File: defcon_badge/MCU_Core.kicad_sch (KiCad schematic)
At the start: 30 parts, among them J33 Dev/SWD header, U2 W25Q16JVUXIQ, U3 RP2040, Y1 ABM8-272-T3

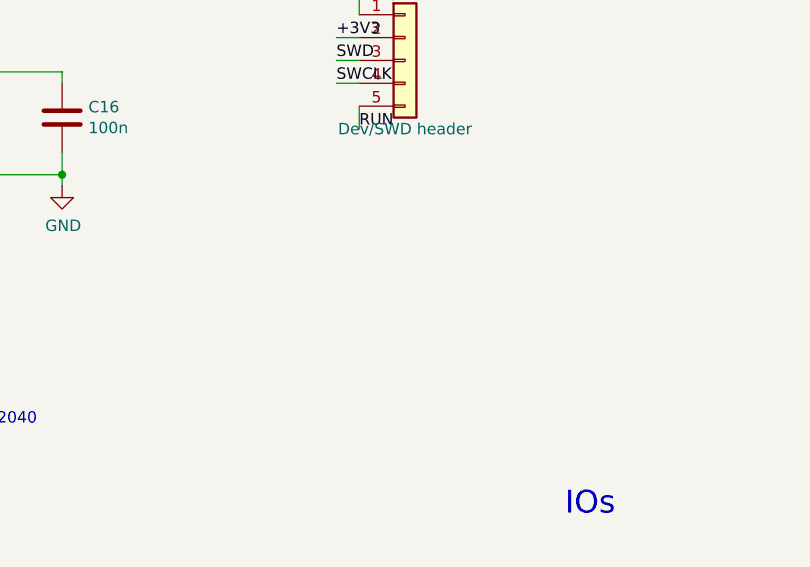
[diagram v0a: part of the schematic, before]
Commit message: Schematic: add RUN 10k pull-up (R6) + wrap-up
- RUN pull-up (R6, 10k RUN->+3V3) per badge_hw_design / RP2040 guide, via a new
  patch script tools/inject_mcu_passives.py (MCU_Core has no generator). Verified
  R6.1->+3V3, R6.2->RUN, ERC 0.
- ADC_AVDD filter: resolved as no-change — a direct ADC_AVDD<->3V3 tie is correct
  best-practice for the badge's coarse VBAT sensing (ferrite+cap only for precision).
- GPIO spares (GP22-25/27-29): waived (intentional unused pins).

Schematic is now electrically correct and ERC-error-clean: every board-killer and
subsystem-fatal bug (power tree, DAC pinout, LED pinout, charger EP) is fixed.
Remaining: microSD card-detect (cross-sheet feature, specced) + the PCB phase
(net re-sync, the SK9822-5050 / TP4056-ESOP8 / microSD-CD footprints, re-place).

Co-Authored-By: Claude Opus 4.8 (1M context) <noreply@anthropic.com>
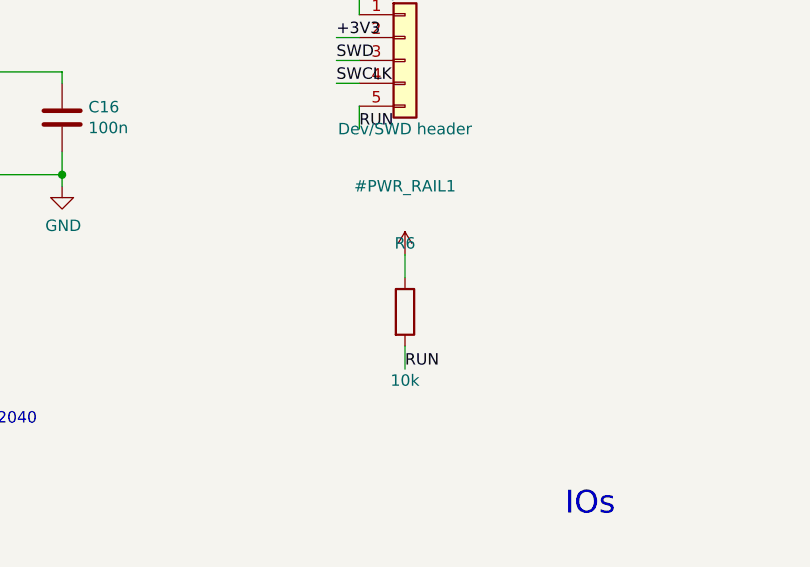
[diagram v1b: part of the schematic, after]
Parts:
- added R6: 10k, Resistor_SMD:R_0402_1005Metric, symbol Device:R
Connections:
- net +3V3: now also R6.1
- net RUN: now also R6.2
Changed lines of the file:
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@@
 		)
 	)
+	(symbol
+		(lib_id "Device:R")
+		(at 330.20 87.63 0)
+		(unit 1)
+		(body_style 1)
+		(exclude_from_sim no)
+		(in_bom yes)
+		(on_board yes)
+		(in_pos_files yes)
+		(dnp no)
+		(fields_autoplaced yes)
+		(property "Reference" "R6" (at 330.20 80.01 0) (effects (font (size 1.27 1.27))))
+		(property "Value" "10k" (at 330.20 95.25 0) (effects (font (size 1.27 1.27))))
+		(property "Footprint" "Resistor_SMD:R_0402_1005Metric" (at 330.20 87.63 0) (show_name no) (hide yes) (effects (font (size 1.27 1.27))))
+		(property "Datasheet" "" (at 330.20 87.63 0) (show_name no) (hide yes) (effects (font (size 1.27 1.27))))
+		(property "Description" "RUN pull-up to +3V3 (RP2040 reset noise immunity)" (at 330.20 87.63 0) (show_name no) (hide yes) (effects (font (size 1.27 1.27))))
+		(pin "1")
+		(pin "2")
+		(instances
+			(project "defcon_badge"
+				(path "/8c0b3d8b-46d3-4173-ab1e-a61765f77d61/614c6d9e-c93d-4105-a0eb-565eebb554cc"
+					(reference "R6")
+					(unit 1)
+				)
+			)
+		)
+	)
+	(symbol
+		(lib_id "power:+3V3")
+		(at 330.20 81.28 0)
+		(unit 1)
+		(body_style 1)
+		(exclude_from_sim no)
+		(in_bom yes)
+		(on_board yes)
+		(in_pos_files yes)
+		(dnp no)
+		(fields_autoplaced yes)
+		(property "Reference" "#PWR_RAIL1" (at 330.20 73.66 0) (effects (font (size 1.27 1.27))))
+		(property "Value" "+3V3" (at 330.20 88.90 0) (effects (font (size 1.27 1.27)) (hide yes)))
+		(property "Footprint" "" (at 330.20 81.28 0) (show_name no) (hide yes) (effects (font (size 1.27 1.27))))
+		(property "Datasheet" "" (at 330.20 81.28 0) (show_name no) (hide yes) (effects (font (size 1.27 1.27))))
+		(property "Description" "" (at 330.20 81.28 0) (show_name no) (hide yes) (effects (font (size 1.27 1.27))))
+		(pin "1")
+		(instances
+			(project "defcon_badge"
+				(path "/8c0b3d8b-46d3-4173-ab1e-a61765f77d61/614c6d9e-c93d-4105-a0eb-565eebb554cc"
+					(reference "#PWR_RAIL1")
+					(unit 1)
+				)
+			)
+		)
+	)
+	(wire (pts (xy 330.20 83.82) (xy 330.20 81.28)) (stroke (width 0) (type default)))
+	(wire (pts (xy 330.20 91.44) (xy 330.20 93.98)) (stroke (width 0) (type default)))
+	(label "RUN" (at 330.20 93.98 0) (effects (font (size 1.27 1.27)) (justify left bottom)))
 )

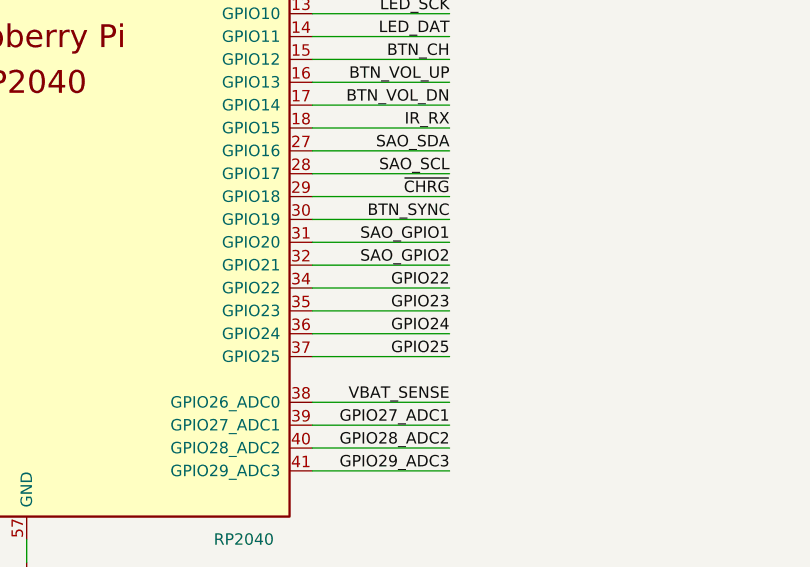
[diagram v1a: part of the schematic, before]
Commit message: Schematic: wire microSD card-detect (SD_CD) + add generator global-label support
Card-detect was unwired ("not wired this rev"). Wired it as a cross-sheet net:
- gen_io_sheet: J31.9 (DET) -> SD_CD with a 10k pull-up (R42) to +3V3. The DET
  switch shorts pin 9 to the grounded shield when a card is inserted, so SD_CD
  reads LOW = card present.
- MCU_Core: repurposed the GP22 spare (U3.34) for SD_CD.
- kicad_sheet_gen: add global-label support (global_label_at_pin / _render_global).
  Used a global label so SD_CD connects across the hierarchy without editing the
  top sheet's sheet-pins/wiring.

Verified: SD_CD = {J31.9, R42.1, U3.34}, R42.2->+3V3, ERC 0 errors.

SCHEMATIC COMPLETE: ERC 0 errors, all board-killers + subsystem-fatal bugs fixed,
4/5 sch_health gates pass (5th = waived GPIO spares). Remaining is the PCB phase.

Co-Authored-By: Claude Opus 4.8 (1M context) <noreply@anthropic.com>
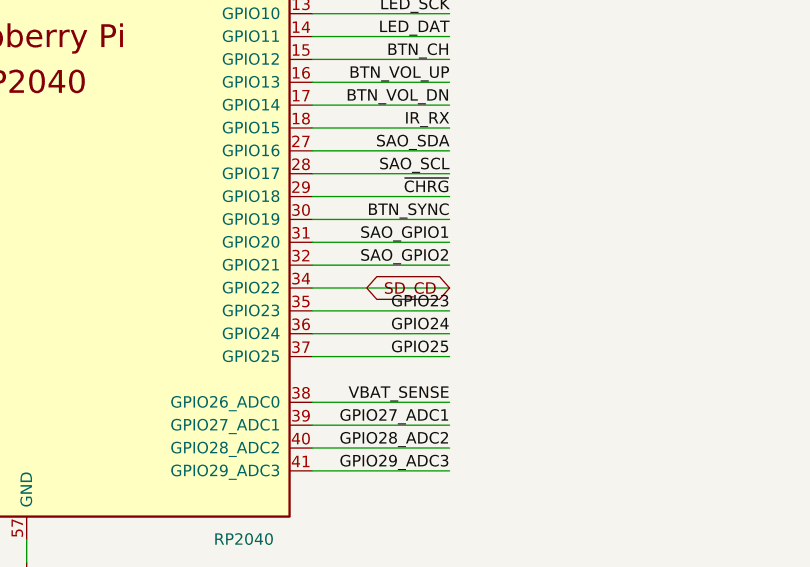
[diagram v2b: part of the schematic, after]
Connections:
- net GPIO22 renamed SD_CD
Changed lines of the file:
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@@
 		)
 	)
-	(label "GPIO22"
+	(global_label "SD_CD"
+		(shape bidirectional)
 		(at 245.11 167.64 180)
 		(effects
@@
 				(size 1.27 1.27)
 			)
-			(justify right bottom)
+			(justify right)
 		)
 	)

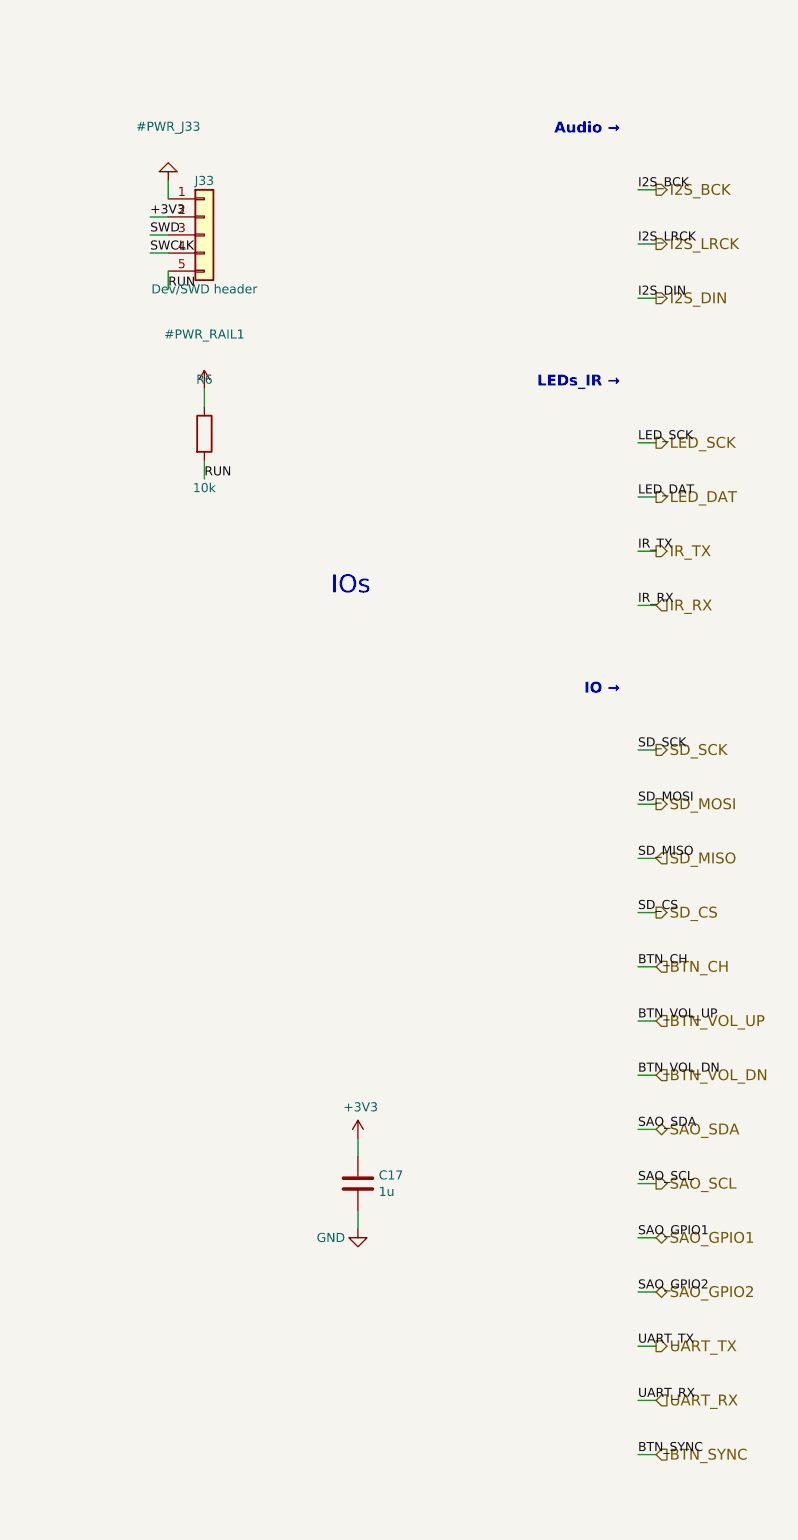
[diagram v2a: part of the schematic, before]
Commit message: Schematic: remove unused J32/J33 debug headers (user request)
The UART debug header (J32, IO sheet) and SWD debug header (J33, MCU_Core)
are unused — the RP2040 is programmed via BOOTSEL/USB (TP1/TP2 pogo pads),
so neither was ever placed on the PCB. Removed both from the schematic so
schematic↔PCB parity stays clean.

Done via a new surgical tool (tools/remove_dev_headers.py) that deletes the
symbols, their power/labels/wires, and the cross-sheet UART plumbing (IO
hier-labels + top-sheet sheet pins + MCU_Core hier-labels/stubs) by
top-level S-expression element, preserving every other symbol UUID (so the
PCB footprint linkage is untouched — no re-sync needed).

The RP2040 debug pins (SWCLK/SWDIO) and UART pins (GP0/GP1) keep their
labels as documented single-pin nets so future test points can attach.

Verified: kicad-cli ERC 0 errors, schematic parity 0 issues. Net warning
delta vs baseline: +4 isolated_pin_label (the intended documented debug
pins), -2 endpoint_off_grid; everything else unchanged.

Co-Authored-By: Claude Opus 4.8 (1M context) <noreply@anthropic.com>
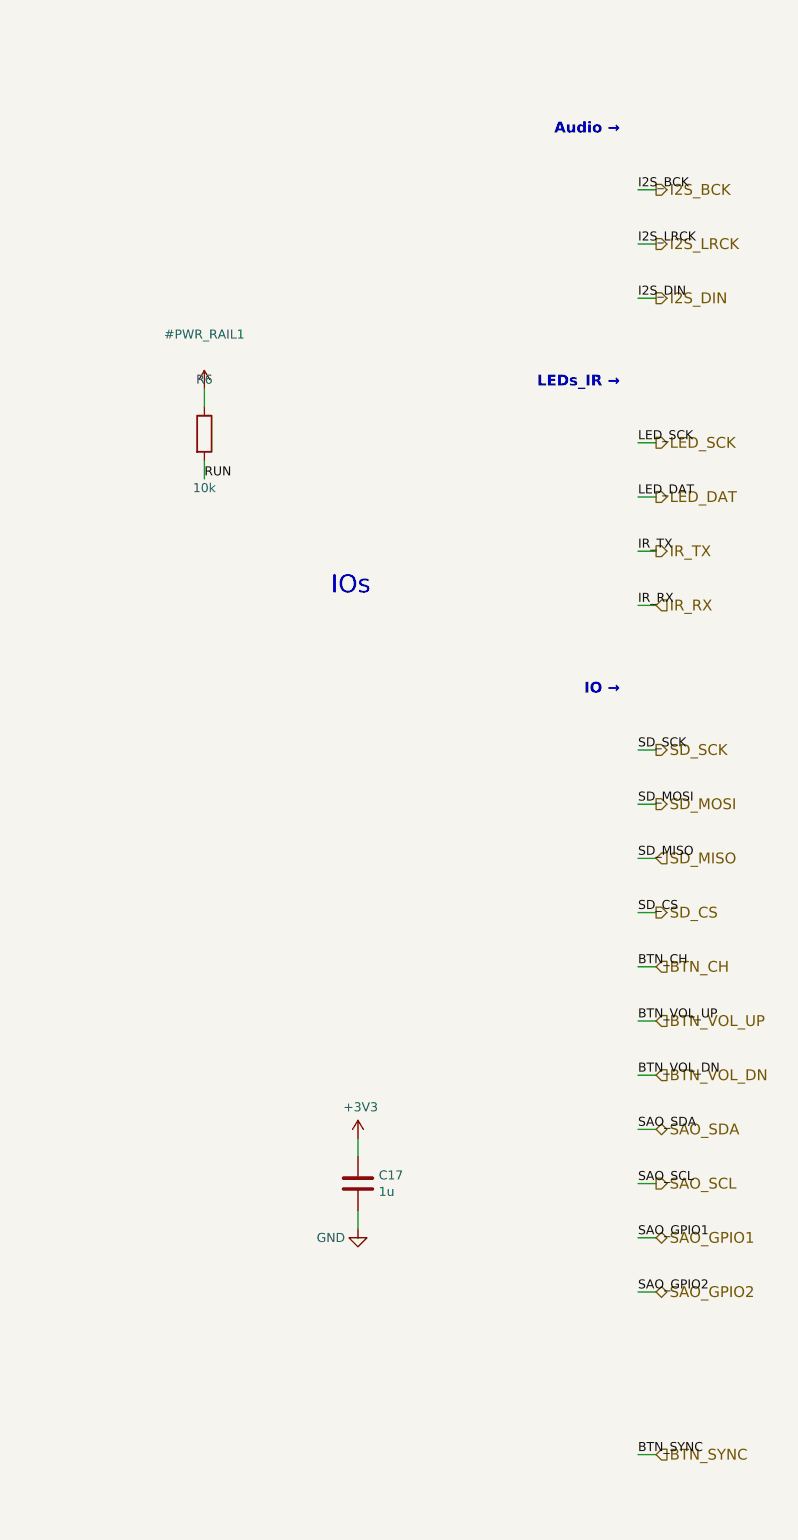
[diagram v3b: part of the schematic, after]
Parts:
- removed J33: Dev/SWD header, Connector_PinHeader_2.54mm:PinHeader_1x05_P2.54mm_Vertical, symbol Connector_Generic:Conn_01x05

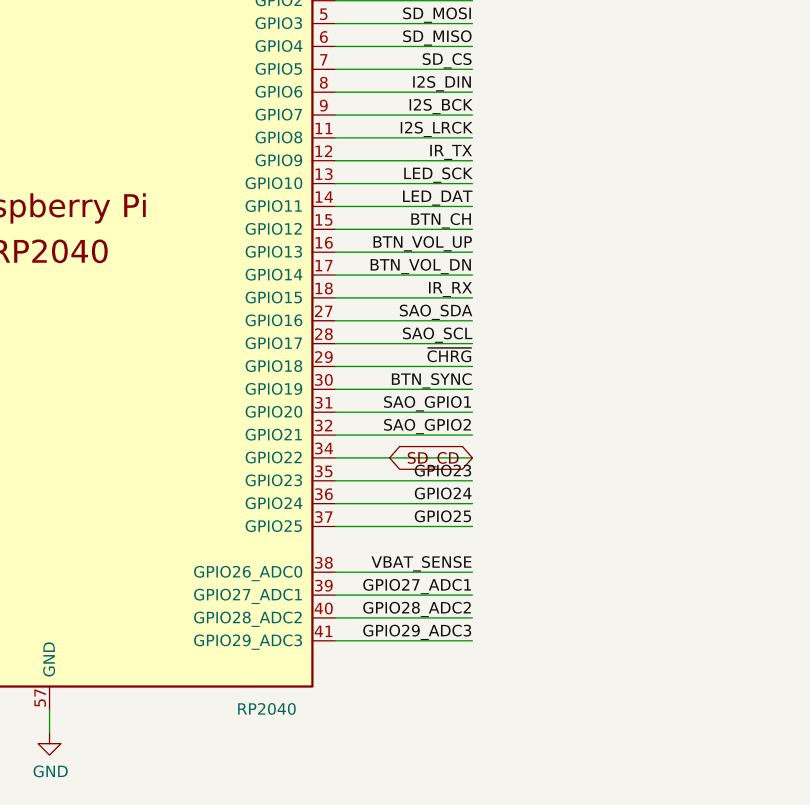
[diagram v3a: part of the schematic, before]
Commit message: R2(1): GPIO remap applied — 6 nets to destination-facing pins (schematic + PCB)
User-authorized firmware-flexible pin remap to dissolve the worst QFN escape
crossings at the source. Built solver (Hungarian + opposite-side penalty + RP2040
pinmux constraints), connectivity resolver (union-find, cross-checked 40/43 pins
vs PCB), and a label-permutation applier (only semantically-correct remap on a
function-named symbol). Moves: LED_SCK GP10->24, LED_DAT GP11->25, IR_RX GP15->27,
SAO_SDA GP16->28, SAO_SCL GP17->29 (GP28/29=hardware I2C0), ~CHRG GP18->10.
I2S left on GP6/7/8 (side-set contiguity). SD_CD dropped (global_label, low value).

Verified: KiCad netlister confirms all 6 nets on intended pins; ERC 73->73 (zero
new); footprint hash unchanged; board clean (via_in_pad 0, drc 0, shorts 0).
Opposite-side crossings 6->1. Firmware must follow the remapped pin map.

Co-Authored-By: Claude Opus 4.8 (1M context) <noreply@anthropic.com>
Claude-Session: https://claude.ai/code/session_01KWhMPfRCULM8VJcQMSwZAy
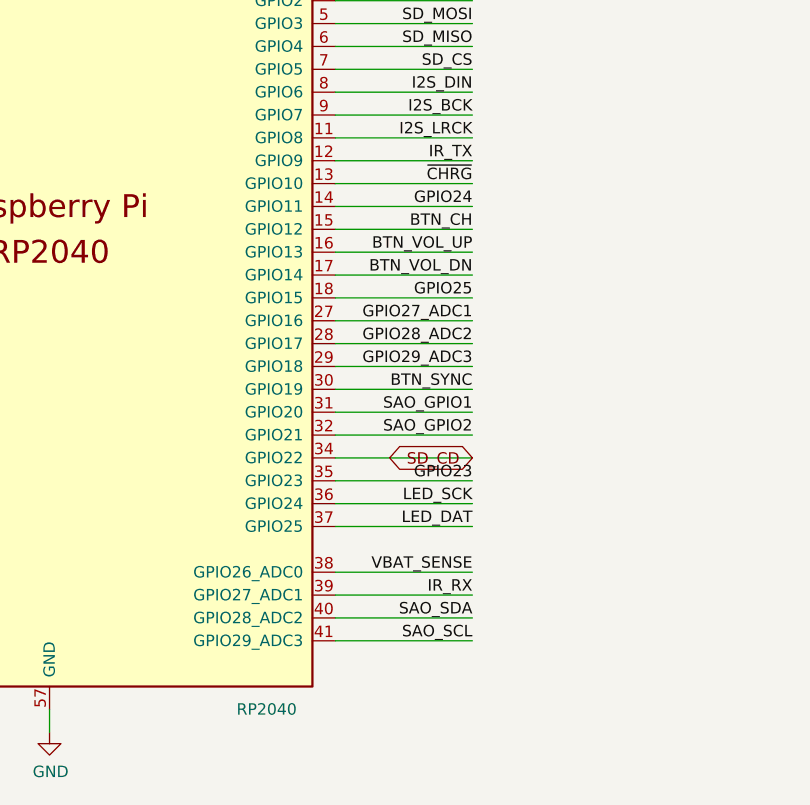
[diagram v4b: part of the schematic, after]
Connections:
- net GPIO24: now also U3.14 (GPIO11); no longer U3.36 (GPIO24)
- net GPIO25: now also U3.18 (GPIO15); no longer U3.37 (GPIO25)
- net GPIO27_ADC1: now also U3.27 (GPIO16); no longer U3.39 (GPIO27_ADC1)
- net GPIO28_ADC2: now also U3.28 (GPIO17); no longer U3.40 (GPIO28_ADC2)
- net GPIO29_ADC3: now also U3.29 (GPIO18); no longer U3.41 (GPIO29_ADC3)
- net IR_RX: now also U3.39 (GPIO27_ADC1); no longer U3.18 (GPIO15)
- net LED_DAT: now also U3.37 (GPIO25); no longer U3.14 (GPIO11)
- net LED_SCK: now also U3.36 (GPIO24); no longer U3.13 (GPIO10)
- net SAO_SCL: now also U3.41 (GPIO29_ADC3); no longer U3.28 (GPIO17)
- net SAO_SDA: now also U3.40 (GPIO28_ADC2); no longer U3.27 (GPIO16)
- net ~{CHRG}: now also U3.13 (GPIO10); no longer U3.29 (GPIO18)
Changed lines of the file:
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@@
 		)
 	)
-	(label "GPIO29_ADC3"
+	(label "SAO_SCL"
 		(at 245.11 187.96 180)
 		(effects
@@
 		)
 	)
-	(label "~{CHRG}"
+	(label "GPIO29_ADC3"
 		(at 245.11 157.48 180)
 		(effects
@@
 		)
 	)
-	(label "GPIO25"
+	(label "LED_DAT"
 		(at 245.11 175.26 180)
 		(effects
@@
 		)
 	)
-	(label "LED_DAT"
+	(label "GPIO24"
 		(at 245.11 139.7 180)
 		(effects
@@
 		)
 	)
-	(label "GPIO27_ADC1"
+	(label "IR_RX"
 		(at 245.11 182.88 180)
 		(effects
@@
 		)
 	)
-	(label "LED_SCK"
+	(label "~{CHRG}"
 		(at 245.11 137.16 180)
 		(effects
@@
 		)
 	)
-	(label "SAO_SCL"
+	(label "GPIO28_ADC2"
 		(at 245.11 154.94 180)
 		(effects
@@
 		)
 	)
-	(label "IR_RX"
+	(label "GPIO25"
 		(at 245.11 149.86 180)
 		(effects
@@
 		)
 	)
-	(label "GPIO24"
+	(label "LED_SCK"
 		(at 245.11 172.72 180)
 		(effects
@@
 		)
 	)
-	(label "GPIO28_ADC2"
+	(label "SAO_SDA"
 		(at 245.11 185.42 180)
 		(effects
@@
 		)
 	)
-	(label "SAO_SDA"
+	(label "GPIO27_ADC1"
 		(at 245.11 152.4 180)
 		(effects
